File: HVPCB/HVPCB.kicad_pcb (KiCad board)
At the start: 2 copper layers, 38 parts, among them U1 NE555DR_C695838, U10 Micro Fit 2P, U2 SN74LVC1GU04DBVR, U3 B0505S-2WR2, U4 LM392MX, U5 AO3400A, U6 AO3400A, U7 KT-0603R, U8 KT-0603R, U9 KT-0603R

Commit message: updated board drawing to add mounting holes, updated test points and moved components to general proximity
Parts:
- added H1: MountingHole, MountingHole:MountingHole_2.2mm_M2, F.Cu at (130.0, 53.6)
- added H2: MountingHole, MountingHole:MountingHole_2.2mm_M2, F.Cu at (130.0, 47.6)
- added H3: MountingHole, MountingHole:MountingHole_2.2mm_M2, F.Cu at (141.9, 53.6)
- added H4: MountingHole, MountingHole:MountingHole_2.2mm_M2, F.Cu at (136.0, 47.6)
- added H5: MountingHole, MountingHole:MountingHole_2.2mm_M2, F.Cu at (141.9, 47.6)
- added H6: MountingHole, MountingHole:MountingHole_2.2mm_M2, F.Cu at (136.0, 53.6)
- added TP2: tp_op_n/i, TestPoint:TestPoint_THTPad_D2.0mm_Drill1.0mm, F.Cu at (222.8, 113.0)
- added TP3: tp_op_out, TestPoint:TestPoint_THTPad_D2.0mm_Drill1.0mm, F.Cu at (231.6, 96.3)
- added TP4: tp_hvStatus, TestPoint:TestPoint_THTPad_D2.0mm_Drill1.0mm, F.Cu at (180.0, 75.0)
- added TP5: tp_Trig, TestPoint:TestPoint_THTPad_D2.0mm_Drill1.0mm, F.Cu at (183.0, 134.0)
- added U11: Micro Fit 2P, footprint:CONN-TH_43045-0200, F.Cu at (134.0, 169.0)
- added U12: Micro Fit 2P, footprint:CONN-TH_43045-0200, F.Cu at (126.0, 183.2)
- added U13: Micro Fit 2P, footprint:CONN-TH_43045-0200, F.Cu at (118.0, 169.0)
- added U14: Micro Fit 2P, footprint:CONN-TH_43045-0200, F.Cu at (118.0, 183.2)
- added U15: Micro Fit 2P, footprint:CONN-TH_43045-0200, F.Cu at (142.0, 169.0)
- added U16: Micro Fit 2P, footprint:CONN-TH_43045-0200, F.Cu at (126.0, 169.0)
- R13, R14: value 10K -> 2K
- R15: value 10K -> 1K
- R20: value 470R -> 10K
- TP1: footprint TestPoint:TestPoint_Pad_D2.0mm -> TestPoint:TestPoint_THTPad_D2.0mm_Drill1.0mm
- moved U3 140.3 mm to (35.0, 103.0)
- moved U9 113.1 mm to (256.3, 25.7)
- moved U10 110.4 mm to (47.0, 122.0), turned to 0 degrees
- moved R7 108.3 mm to (248.4, 27.2)
- moved C5 107.5 mm to (249.2, 32.3)
- moved R6 106.5 mm to (248.3, 36.8)
- moved R1 97.2 mm to (222.2, 34.0)
- moved C4 96.2 mm to (222.2, 42.7)
- moved U8 90.5 mm to (230.1, 39.1)
- moved R4 88.8 mm to (222.2, 39.1)
- moved U5 59.0 mm to (256.5, 32.5)
- moved U6 48.9 mm to (227.8, 28.4)
- moved R18 45.5 mm to (224.5, 105.9)
- moved U4 45.3 mm to (214.1, 111.5)
- moved R17 41.9 mm to (204.0, 111.8)
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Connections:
- R1 pad 2: HV_PULSE -> /PULSE
- R4 pad 1: HV_PULSE -> /PULSE
- U10 pad 1: unconnected-(U10-Pad1) -> R_TSAL
- U10 pad 2: unconnected-(U10-Pad2) -> GND
- U5 pad 3: GREEN_TSAL -> G_TSAL
- U6 pad 3: RED_TSAL -> R_TSAL
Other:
- board outline added: 140 x 60 mm

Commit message: added mounting holes and organized board
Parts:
- U3: value B0505S-2WR2 -> PDSE1-S5-D5-M-TR; footprint footprint:PWRM-TH_BXXXXS-2WR2 -> Converter_DCDC:CUI Isolated DC-DC
- moved TP1 175.1 mm to (106.0, 90.0)
- moved C1 174.6 mm to (97.4, 94.7)
- moved D2 174.6 mm to (99.6, 95.4)
- moved R2 174.6 mm to (96.4, 91.2)
- moved R3 174.6 mm to (100.2, 91.2)
- moved S1 174.3 mm to (96.3, 85.8), turned to -90 degrees
- moved H1 129.9 mm to (19.0, 121.0)
- moved H5 125.1 mm to (19.0, 71.0)
- moved H6 80.4 mm to (92.2, 121.0)
- moved H3 67.8 mm to (149.0, 121.0)
- moved H4 49.6 mm to (92.2, 71.0)
- moved H2 30.1 mm to (149.0, 71.0)
- moved U3 6.99 mm to (28.5, 105.7)
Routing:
- net ~{Discharge}: track 0.00 -> 5.39 mm
- net +5V: track 0.00 -> 2.33 mm
- net /S1_ls: track 0.00 -> 2.24 mm

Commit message: progress on layout
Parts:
- removed U10, U11, U12, U13, U15: Micro Fit 2P, footprint:CONN-TH_43045-0200
- added J1: Micro Fit 10p, Connector_Molex:Molex_Micro-Fit_3.0_43650-1010_1x10-1MP_P3.00mm_Horizontal, F.Cu at (150.7, 96.1)
- added Q1: OnSemi FDB12N50TM, Package_TO_SOT_SMD:TO-263-2_TabPin1_D2PAK, F.Cu at (40.4, 94.5)
- added R8: 1K, Resistor_SMD:R_0603_1608Metric_Pad0.98x0.95mm_HandSolder, F.Cu at (49.0, 86.8)
- added R9: 1K, Resistor_SMD:R_0603_1608Metric_Pad0.98x0.95mm_HandSolder, F.Cu at (49.9, 83.0)
- moved TP2 151.4 mm to (71.5, 106.7)
- moved R13 149.8 mm to (78.2, 99.2), turned to 180 degrees
- moved R14 147.0 mm to (75.3, 100.1), turned to -90 degrees
- moved R15 143.3 mm to (72.5, 99.2), turned to 180 degrees
- moved U7 140.6 mm to (89.8, 103.4), turned to -90 degrees
- moved S2 139.3 mm to (106.9, 106.0), turned to 180 degrees
- moved R19 139.1 mm to (99.7, 104.6)
- moved TP3 137.4 mm to (94.5, 104.5)
- moved U16 137.2 mm to (17.2, 85.3), turned to -90 degrees
- moved R18 134.8 mm to (89.8, 99.3), turned to -90 degrees
- moved R5 133.1 mm to (85.1, 101.9)
- moved U4 130.4 mm to (83.7, 107.6), turned to 180 degrees
- moved U14 128.2 mm to (17.2, 104.0), turned to -90 degrees
- moved R16 126.4 mm to (78.2, 105.6), turned to -90 degrees
- moved R20 126.0 mm to (112.8, 108.3), turned to 90 degrees
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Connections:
- S1 pad 3: /res_net_conn -> Net-(S1-Pad3)
- S1 pad 4: HV+ -> HV_5V
- U16 pad 1: /res_net_conn -> HV-
- U16 pad 2: HV- -> Net-(U16-Pad2)
- U3 pad 5: (no net) -> HV_5V
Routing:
- net Net-(U16-Pad2): track 0.00 -> 17.4 mm
- net /op_n/i: track 0.00 -> 15.5 mm
- net 1V_REF: track 0.00 -> 14.8 mm
- net Net-(R8-Pad2): track 0.00 -> 13.8 mm
- net /op_out: track 0.00 -> 12.1 mm
- net HV_STATUS: track 0.00 -> 4.75 mm
- net Net-(C5-Pad1): track 0.00 -> 4.74 mm
- net Net-(C4-Pad1): track 0.00 -> 4.72 mm
- net /sFeed: track 0.00 -> 3.11 mm
- net HV-: track 0.00 -> 2.66 mm
- net Net-(S1-Pad3): track 0.00 -> 2.40 mm
- net /hvSled: track 0.00 -> 2.36 mm
- net Net-(R6-Pad1): track 0.00 -> 2.15 mm
- net Net-(R1-Pad1): track 0.00 -> 2.14 mm
- net /PULSE: track 0.00 -> 1.98 mm
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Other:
- board text added: "1V REF"

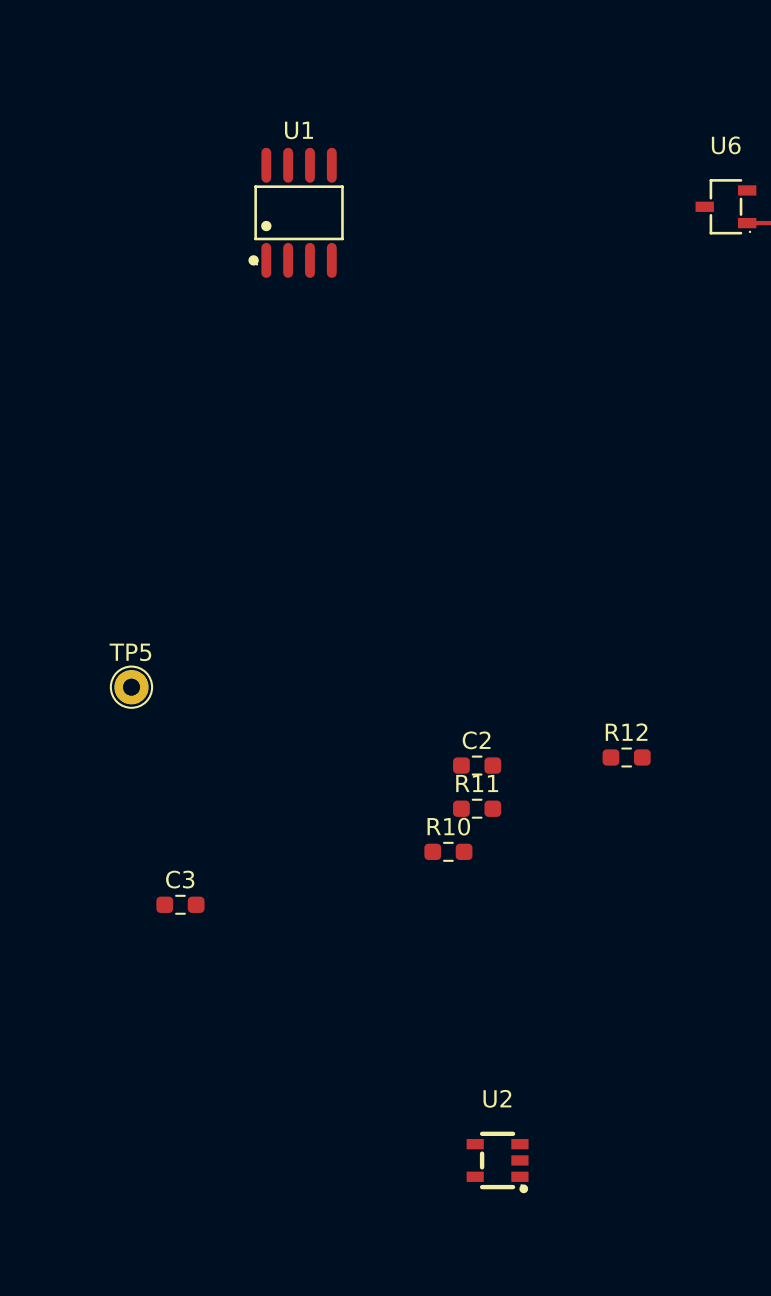
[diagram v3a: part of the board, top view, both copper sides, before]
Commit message: routing of 555 timer
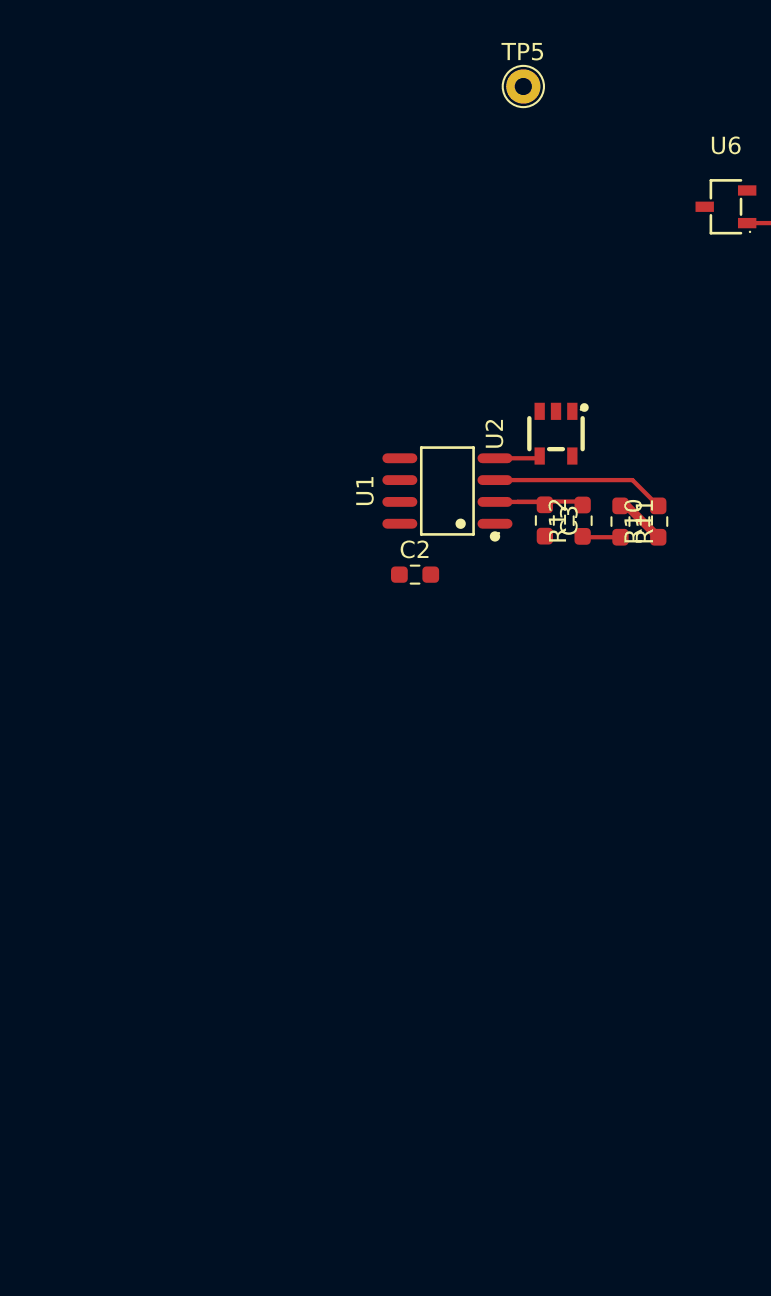
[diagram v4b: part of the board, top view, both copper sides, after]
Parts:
- moved U2 42.4 mm to (217.9, 41.6), turned to 90 degrees
- moved TP5 41.7 mm to (216.1, 21.4)
- moved C3 30.8 mm to (217.3, 46.7), turned to -90 degrees
- moved R10 22.8 mm to (223.9, 46.8), turned to 90 degrees
- moved R11 18.7 mm to (221.7, 46.8), turned to -90 degrees
- moved U1 18.3 mm to (211.6, 45.0), turned to 90 degrees
- moved R12 14.0 mm to (219.5, 46.7), turned to 90 degrees
- moved C2 11.7 mm to (209.8, 49.9)
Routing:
- net /PULSE: track 1.98 -> 12.1 mm
- net /TRIG: track 0.00 -> 6.96 mm
- net +5V: track 2.33 -> 5.28 mm
- net Net-(U1-Pad4): track 0.00 -> 2.65 mm
- net Net-(R11-Pad2): track 0.00 -> 2.22 mm

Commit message: layout almost done
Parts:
- moved R6 179.8 mm to (91.2, 102.5), turned to 0 degrees
- moved U9 179.0 mm to (90.3, 99.5), turned to -90 degrees
- moved R7 173.7 mm to (94.1, 101.5), turned to 90 degrees
- moved C5 172.9 mm to (93.2, 98.5), turned to 180 degrees
- moved U5 166.8 mm to (97.8, 101.5), turned to 180 degrees
- moved R10 159.0 mm to (74.7, 101.8), turned to 0 degrees
- moved R1 156.6 mm to (91.3, 90.8), turned to 0 degrees
- moved R11 156.2 mm to (74.7, 99.6), turned to 180 degrees
- moved U8 155.8 mm to (90.4, 87.8), turned to -90 degrees
- moved R12 153.3 mm to (74.8, 97.4), turned to 0 degrees
- moved R4 150.6 mm to (94.2, 89.9), turned to 90 degrees
- moved C4 149.9 mm to (93.2, 86.9), turned to 180 degrees
- moved U2 149.4 mm to (79.7, 98.4), turned to 0 degrees
- moved TP5 147.4 mm to (83.9, 86.8), turned to -90 degrees
- moved C3 145.0 mm to (77.9, 86.7), turned to 0 degrees
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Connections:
- J1 pad 4: HV_STATUS -> +5V
- J1 pad 6: +5V -> R_TSAL
- J1 pad 7: GND -> G_TSAL
- J1 pad 8: G_TSAL -> GND
- J1 pad 9: R_TSAL -> HV_STATUS
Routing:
- net +5V: track 5.28 -> 159.4 mm
- net HV_STATUS: track 4.75 -> 99.2 mm
- net ~{Discharge}: track 5.39 -> 90.1 mm
- net R_TSAL: track 0.00 -> 52.3 mm
- net G_TSAL: track 0.00 -> 46.8 mm
- net /PULSE: track 12.1 -> 26.8 mm
- net /TRIG: track 6.96 -> 20.2 mm
- net Net-(R11-Pad2): track 2.22 -> 11.7 mm
- net 1V_REF: track 14.8 -> 9.07 mm
- net /op_n/i: track 15.5 -> 19.9 mm
- net Net-(U16-Pad2): track 17.4 -> 19.5 mm
- net Net-(R13-Pad2): track 1.95 -> 0.00 mm
- net /op_out: track 12.1 -> 13.4 mm
- net /sFeed: track 3.11 -> 2.46 mm

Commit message: finished layout
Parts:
- moved R13 65.2 mm to (101.8, 103.6)
- moved R14 65.0 mm to (98.7, 104.5)
- moved C1 65.0 mm to (130.4, 80.7)
- moved C5 65.0 mm to (158.2, 96.0)
- moved C2 65.0 mm to (139.0, 84.2)
- moved C4 65.0 mm to (158.2, 84.4)
- moved D1 65.0 mm to (110.8, 113.8)
- moved D2 65.0 mm to (131.1, 78.4)
- moved H1 65.0 mm to (84.0, 118.5)
- moved H2 65.0 mm to (214.0, 68.5)
- moved H3 65.0 mm to (214.0, 118.5)
- moved H4 65.0 mm to (157.2, 68.5)
- moved H5 65.0 mm to (84.0, 68.5)
- moved H6 65.0 mm to (157.2, 118.5)
- moved J1 65.0 mm to (215.7, 93.6)
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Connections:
- Q1 pad 3: Net-(U16-Pad2) -> Net-(Q1-Pad3)
- U14 pad 1: HV- -> HV+
- U14 pad 2: HV+ -> HV-
- U16 pad 1: HV- -> Net-(Q1-Pad3)
- U16 pad 2: Net-(U16-Pad2) -> HV-
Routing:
- net HV+: track 0.00 -> 89.8 mm
- net HV_5V: track 0.00 -> 61.4 mm
- net Net-(Q1-Pad3): track 0.00 -> 28.3 mm
- net Net-(U16-Pad2): track 19.5 -> 0.00 mm
- net Net-(R13-Pad2): track 0.00 -> 2.13 mm
- net /hvSled: track 2.36 -> 3.22 mm
- net HV-: vias 0 -> 21
- net GND: vias 0 -> 71
- added copper zone on B.Cu, net GND
- added copper zone on F.Cu, net GND
- added copper zone on B.Cu, net HV-
- added copper zone on F.Cu, net HV-
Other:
- board text removed: "1V REF"

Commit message: HVPCB updates & assembly files
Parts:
- removed C1: 100nF, Resistor_SMD:R_0603_1608Metric_Pad0.98x0.95mm_HandSolder
- removed D2: 5V, footprint:LL-34_L3.5-W1.5-RD
- removed Q1: OnSemi FDB12N50TM, Package_TO_SOT_SMD:TO-263-2_TabPin1_D2PAK
- removed R2, R3: 10K, Resistor_SMD:R_0603_1608Metric_Pad0.98x0.95mm_HandSolder
- removed R8, R9: 1K, Resistor_SMD:R_0603_1608Metric_Pad0.98x0.95mm_HandSolder
- removed S1: KAQY414S, footprint:SOP-4_L3.9-W4.4-P2.54-LS7.0-BR
- removed TP1: tp_Discharge, TestPoint:TestPoint_THTPad_D2.0mm_Drill1.0mm
- removed U16: Micro Fit 2P, footprint:CONN-TH_43045-0200
- C2, C3, C4, C5: footprint Resistor_SMD:R_0603_1608Metric_Pad0.98x0.95mm_HandSolder -> Capacitor_SMD:C_0603_1608Metric_Pad1.08x0.95mm_HandSolder
- D1: value 5V -> 5v ZMM5V6-M; footprint footprint:LL-34_L3.5-W1.5-RD -> Diode_SMD:D_MiniMELF
- J1: value Micro Fit 10p -> MicroFit_8p; footprint Connector_Molex:Molex_Micro-Fit_3.0_43650-1010_1x10-1MP_P3.00mm_Horizontal -> Connector_Molex:Molex_Micro-Fit_3.0_43650-0800_1x08_P3.00mm_Horizontal
- moved R15 22.3 mm to (108.3, 85.6), turned to 0 degrees
- moved R16 21.8 mm to (97.2, 96.3), turned to -90 degrees
- moved TP2 20.4 mm to (97.8, 104.1), turned to 90 degrees
- moved U4 20.0 mm to (101.6, 91.2), turned to 90 degrees
- moved R14 19.3 mm to (108.2, 87.7), turned to 180 degrees
- moved D1 18.3 mm to (98.7, 100.0), turned to 0 degrees
- moved R17 17.8 mm to (99.9, 97.2), turned to 0 degrees
- moved R13 14.8 mm to (109.2, 90.8), turned to 90 degrees
- moved R5 13.6 mm to (107.2, 92.5), turned to -90 degrees
- moved R19 11.7 mm to (104.1, 103.8), turned to -90 degrees
- moved J1 11.3 mm to (211.5, 83.1)
- moved U7 11.1 mm to (105.2, 96.8), turned to 180 degrees
- moved TP3 11.1 mm to (104.1, 99.8), turned to -90 degrees
- moved R18 8.37 mm to (109.1, 95.7), turned to -90 degrees
- moved U14 7.70 mm to (82.5, 93.8)
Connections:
- J1 pad 2: ~{Discharge} -> +5V
- J1 pad 4: +5V -> R_TSAL
- J1 pad 5: GND -> G_TSAL
- J1 pad 6: R_TSAL -> GND
- J1 pad 7: G_TSAL -> HV_STATUS
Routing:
- net ~{Discharge}: track 90.1 -> 0.00 mm
- net HV+: track 89.8 -> 12.6 mm
- net Net-(Q1-Pad3): track 28.3 -> 0.00 mm
- net HV_5V: track 61.4 -> 40.5 mm
- net Net-(R8-Pad2): track 13.8 -> 0.00 mm
- net /sFeed: track 2.46 -> 15.7 mm
- net +5V: track 159.4 -> 148.8 mm
- net R_TSAL: track 52.3 -> 49.2 mm
- net HV-: track 2.66 -> 0.11 mm, vias 21 -> 20
- net Net-(S1-Pad3): track 2.40 -> 0.00 mm
- net /S1_ls: track 2.24 -> 0.00 mm
- net G_TSAL: track 46.8 -> 49.0 mm
- net /op_n/i: track 19.9 -> 21.0 mm
- net GND: vias 71 -> 72
- removed copper zone on F.Cu, net /S1_ls
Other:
- board text added: "5V"
- board text added: "G_TSAL"
- board text added: "G_TSAL (<60V)"
- board text added: "HV+/HV-"
- board text added: "LHRE - HVPCB - 12/10/2022"
- board text added: "LV ZONE"
- board text added: "R_TSAL"
- board text added: "R_TSAL (>60V)"
- board text added: "TSV IND."
- board text added: "TS_STATUS"
- board text added: "rev. 1"

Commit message: updates to silkscreen for HVPCB
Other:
- board text added: "GND Unless Noted"
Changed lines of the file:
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@@
       (outputformat 1)
       (mirror false)
-      (drillshape 1)
+      (drillshape 0)
       (scaleselection 1)
-      (outputdirectory "")
+      (outputdirectory "Assembly/")
     )
   )
@@
     (pad "" np_thru_hole circle (at 2.15 -4.32 270) (size 3 3) (drill 3) (layers *.Cu *.Mask))
     (pad "" np_thru_hole circle (at 18.85 -4.32 270) (size 3 3) (drill 3) (layers *.Cu *.Mask))
-    (pad "1" thru_hole roundrect (at 0 0 270) (size 1.5 2.02) (drill 1.02) (layers *.Cu *.Mask) (roundrect_rratio 0.166667)
+    (pad "1" thru_hole roundrect (at 0 0 270) (size 1.5 2.02) (drill 1.02) (layers *.Cu *.Mask) (roundrect_rratio 0.1666673333)
       (net 1 "GND") (pinfunction "Pin_1") (pintype "passive"))
     (pad "2" thru_hole oval (at 3 0 270) (size 1.5 2.02) (drill 1.02) (layers *.Cu *.Mask)
@@
   (gr_arc (start 214 63.5) (mid 217.535534 64.964466) (end 219 68.5) (layer "Edge.Cuts") (width 0.1))
   (gr_line (start 214 123.5) (end 84 123.5) (layer "Edge.Cuts") (width 0.1))
-  (gr_text "TS_STATUS\n" (at 203.1 99.6) (layer "F.SilkS")
+  (gr_text "TS_STATUS\n" (at 203.3 99.8) (layer "F.SilkS")
     (effects (font (size 1.5 1.5) (thickness 0.3)))
   )
@@
     (effects (font (size 1.5 1.5) (thickness 0.3)))
   )
-  (gr_text "R_TSAL\n" (at 205.2 89.2) (layer "F.SilkS")
+  (gr_text "R_TSAL\n" (at 205.2 92.1) (layer "F.SilkS")
     (effects (font (size 1.5 1.5) (thickness 0.3)))
   )
-  (gr_text "G_TSAL\n" (at 205.1 94.5) (layer "F.SilkS")
+  (gr_text "G_TSAL\n" (at 205.4 94.8) (layer "F.SilkS")
     (effects (font (size 1.5 1.5) (thickness 0.3)))
   )
@@
     (effects (font (size 2 2) (thickness 0.3)))
   )
+  (gr_text "GND Unless Noted" (at 211 78.2) (layer "F.SilkS")
+    (effects (font (size 1 1) (thickness 0.15)))
+  )
   (gr_text "TSV IND." (at 106.8 107.8) (layer "F.SilkS")
